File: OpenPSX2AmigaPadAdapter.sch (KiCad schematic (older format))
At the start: 42 parts, among them J1 TO_PSX_PAD, J2 DB9_F, J3 CONN_FTDI, J4 CONN_ICSP, J99 OSHW_LOGO, Q1 BSS138, Q2 BSS138, Q3 BSS138, Q4 BSS138, SW1 RESET, U1 ATmega328P-AU, U2 LM1117-3.3, Y1 16M, Y2 16M

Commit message: Final PCB fixes for V2
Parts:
- renumbered C2 to C1, C8 to C10, C1 to C2, C6 to C3, C7 to C4, C4 to C6, C3 to C7, C9 to C8, C10 to C9, LD2 to LD1, LD1 to LD2, R15 to R11, R14 to R12, R12 to R14, R11 to R15
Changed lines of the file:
@@
 	3545 2685 3465 2685
 $Comp
-L Device:C C8
+L Device:C C10
 U 1 1 5D1C8DC2
 P 3330 2905
-F 0 "C8" V 3280 3005 50  0000 C CNN
+F 0 "C10" V 3280 3030 50  0000 C CNN
 F 1 "100n" V 3385 3055 50  0000 C CNN
 F 2 "Capacitor_SMD:C_0805_2012Metric_Pad1.15x1.40mm_HandSolder" H 3368 2755 50  0001 C CNN
@@
 NoConn ~ 2390 2505
 $Comp
-L Device:LED LD1
+L Device:LED LD2
 U 1 1 5D311FEE
 P 4775 5375
-F 0 "LD1" H 4768 5211 50  0000 C CNN
+F 0 "LD2" H 4768 5211 50  0000 C CNN
 F 1 "LED" H 4768 5211 50  0001 C CNN
 F 2 "LED_SMD:LED_0805_2012Metric_Pad1.15x1.40mm_HandSolder" H 4775 5375 50  0001 C CNN
@@
 	2390 2305 2720 2305
 Text Label 2460 2305 0    50   ~ 0
+led2
+Text Label 2460 2405 0    50   ~ 0
 led1
-Text Label 2460 2405 0    50   ~ 0
-led2
 $Comp
 L power:GND #PWR027
@@
 $EndComp
 $Comp
-L Device:LED LD2
+L Device:LED LD1
 U 1 1 5D332AA0
 P 4775 5575
-F 0 "LD2" H 4768 5699 50  0000 C CNN
+F 0 "LD1" H 4768 5699 50  0000 C CNN
 F 1 "LED" H 4768 5789 50  0001 C CNN
 F 2 "LED_SMD:LED_0805_2012Metric_Pad1.15x1.40mm_HandSolder" H 4775 5575 50  0001 C CNN
@@
 	5075 5575 5075 5670
 $Comp
-L Device:R R11
+L Device:R R15
 U 1 1 5D343268
 P 4340 5375
-F 0 "R11" V 4133 5375 50  0000 C CNN
+F 0 "R15" V 4133 5375 50  0000 C CNN
 F 1 "220" V 4224 5375 50  0000 C CNN
 F 2 "Resistor_SMD:R_0805_2012Metric_Pad1.15x1.40mm_HandSolder" V 4270 5375 50  0001 C CNN
@@
 $EndComp
 $Comp
-L Device:R R12
+L Device:R R14
 U 1 1 5D343E5C
 P 4340 5575
-F 0 "R12" V 4455 5575 50  0000 C CNN
+F 0 "R14" V 4455 5575 50  0000 C CNN
 F 1 "220" V 4546 5575 50  0000 C CNN
 F 2 "Resistor_SMD:R_0805_2012Metric_Pad1.15x1.40mm_HandSolder" V 4270 5575 50  0001 C CNN
@@
 Wire Wire Line
 	4190 5575 3920 5575
-Text Label 3920 5375 0    50   ~ 0
-led1
-Text Label 3920 5575 0    50   ~ 0
-led2
 Wire Wire Line
 	1310 5905 1660 5905
@@
 $EndComp
 $Comp
-L Device:C C4
+L Device:C C6
 U 1 1 5D3D42CF
 P 1310 6205
-F 0 "C4" H 1275 6120 50  0000 R CNN
+F 0 "C6" H 1275 6120 50  0000 R CNN
 F 1 "100n" H 1280 6315 50  0000 R CNN
 F 2 "Capacitor_SMD:C_0805_2012Metric_Pad1.15x1.40mm_HandSolder" H 1348 6055 50  0001 C CNN
@@
 $EndComp
 $Comp
-L Device:C C3
+L Device:C C7
 U 1 1 5D3D4648
 P 1660 6205
-F 0 "C3" H 1620 6120 50  0000 R CNN
+F 0 "C7" H 1620 6120 50  0000 R CNN
 F 1 "100n" H 1625 6315 50  0000 R CNN
 F 2 "Capacitor_SMD:C_0805_2012Metric_Pad1.15x1.40mm_HandSolder" H 1698 6055 50  0001 C CNN
@@
 $EndComp
 $Comp
-L Device:C C1
+L Device:C C2
 U 1 1 5D3DD729
 P 2010 6205
-F 0 "C1" H 1975 6115 50  0000 R CNN
+F 0 "C2" H 1975 6115 50  0000 R CNN
 F 1 "10u" H 1985 6315 50  0000 R CNN
 F 2 "Capacitor_SMD:C_1206_3216Metric_Pad1.42x1.75mm_HandSolder" H 2048 6055 50  0001 C CNN
@@
 $EndComp
 $Comp
-L Device:C C2
+L Device:C C1
 U 1 1 5D3DDD18
 P 3210 6205
-F 0 "C2" H 3175 6115 50  0000 R CNN
+F 0 "C1" H 3175 6115 50  0000 R CNN
 F 1 "10u" H 3175 6320 50  0000 R CNN
 F 2 "Capacitor_SMD:C_1206_3216Metric_Pad1.42x1.75mm_HandSolder" H 3248 6055 50  0001 C CNN
@@
 FOR ICSP
 $Comp
-L Device:C C6
+L Device:C C3
 U 1 1 5D19A701
 P 4205 2005
-F 0 "C6" V 3953 2005 50  0000 C CNN
+F 0 "C3" V 3953 2005 50  0000 C CNN
 F 1 "22p" V 4044 2005 50  0000 C CNN
 F 2 "Capacitor_SMD:C_0805_2012Metric_Pad1.15x1.40mm_HandSolder" H 4243 1855 50  0001 C CNN
@@
 	4510 2305 4510 2505
 $Comp
-L Device:C C7
+L Device:C C4
 U 1 1 5D1A882F
 P 4205 2305
-F 0 "C7" V 4365 2305 50  0000 C CNN
+F 0 "C4" V 4365 2305 50  0000 C CNN
 F 1 "22p" V 4456 2305 50  0000 C CNN
 F 2 "Capacitor_SMD:C_0805_2012Metric_Pad1.15x1.40mm_HandSolder" H 4243 2155 50  0001 C CNN
@@
 	8710 4880 9895 4880
 $Comp
-L Device:R R15
+L Device:R R11
 U 1 1 5DAF3262
 P 9655 1920
-F 0 "R15" H 9820 1770 50  0000 R CNN
+F 0 "R11" H 9820 1770 50  0000 R CNN
 F 1 "10k" V 9655 1990 50  0000 R CNN
 F 2 "Resistor_SMD:R_0805_2012Metric_Pad1.15x1.40mm_HandSolder" V 9585 1920 50  0001 C CNN
@@
 $EndComp
 $Comp
-L Device:R R14
+L Device:R R12
 U 1 1 5DAFD7E8
 P 9395 1930
-F 0 "R14" H 9555 1780 50  0000 R CNN
+F 0 "R12" H 9555 1780 50  0000 R CNN
 F 1 "10k" V 9395 2005 50  0000 R CNN
 F 2 "Resistor_SMD:R_0805_2012Metric_Pad1.15x1.40mm_HandSolder" V 9325 1930 50  0001 C CNN
@@
 	9395 2900 8745 2900
 $Comp
-L Device:C C10
+L Device:C C9
 U 1 1 5DB50106
 P 9655 3235
-F 0 "C10" H 9770 3281 50  0000 L CNN
-F 1 "220p" H 9770 3190 50  0000 L CNN
+F 0 "C9" H 9660 3320 50  0000 L CNN
+F 1 "220p" H 9665 3150 50  0000 L CNN
 F 2 "Capacitor_SMD:C_0805_2012Metric_Pad1.15x1.40mm_HandSolder" H 9693 3085 50  0001 C CNN
 F 3 "~" H 9655 3235 50  0001 C CNN
@@
 $EndComp
 $Comp
-L Device:C C9
+L Device:C C8
 U 1 1 5DB5B8E8
 P 9395 3235
-F 0 "C9" H 9280 3281 50  0000 R CNN
-F 1 "820p" H 9280 3190 50  0000 R CNN
+F 0 "C8" H 9505 3320 50  0000 R CNN
+F 1 "820p" H 9590 3145 50  0000 R CNN
 F 2 "Capacitor_SMD:C_0805_2012Metric_Pad1.15x1.40mm_HandSolder" H 9433 3085 50  0001 C CNN
 F 3 "~" H 9395 3235 50  0001 C CNN
@@
 	9395 3575 9655 3575
 Connection ~ 9655 3575
+Text Label 3920 5575 0    50   ~ 0
+led1
+Text Label 3920 5375 0    50   ~ 0
+led2
 $EndSCHEMATC

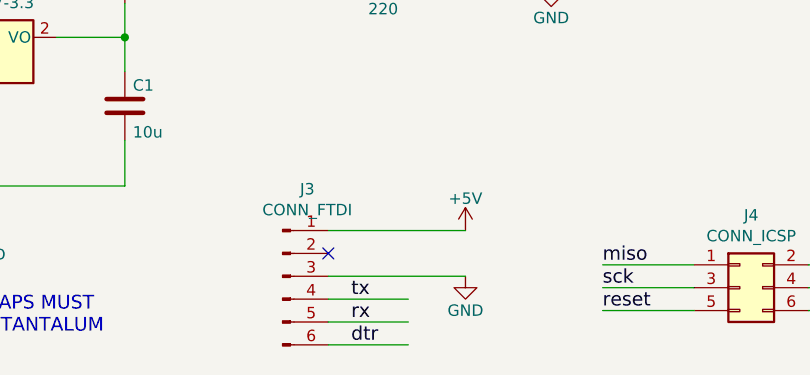
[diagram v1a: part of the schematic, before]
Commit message: Use handsoldering footprints and fix FTDI connector
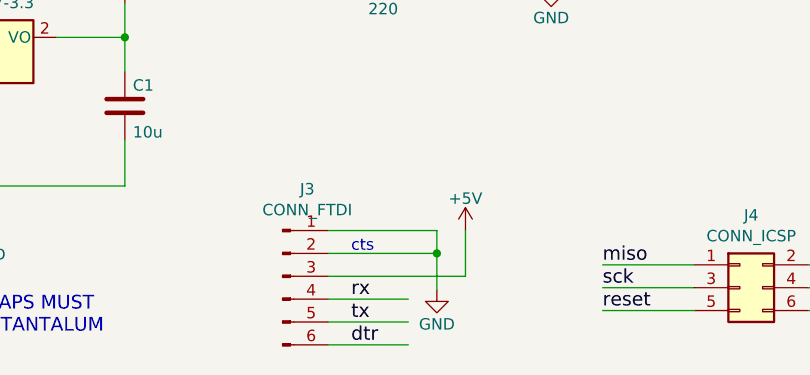
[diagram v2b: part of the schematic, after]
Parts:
- Q1, Q2, Q3, Q4: footprint Package_TO_SOT_SMD:SOT-23 -> Package_TO_SOT_SMD:SOT-23_Handsoldering
- SW1: footprint Button_Switch_SMD:SW_SPST_EVPBF -> Button_Switch_SMD:SW_SPST_EVQQ2
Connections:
- wire segments 189 -> 193
- no-connect marks 11 -> 10
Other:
- note added: "cts"
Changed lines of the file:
@@
 EESchema Schematic File Version 4
-LIBS:OpenPSX2AmigaPadAdapter-cache
-EELAYER 29 0
+EELAYER 30 0
 EELAYER END
 $Descr A4 11693 8268
@@
 Sheet 1 1
 Title "OpenPSX2AmigaPadAdapter"
-Date "2019-10-29"
-Rev "2"
+Date "2019-12-10"
+Rev "3"
 Comp "SukkoPera"
 Comment1 "Licensed under CERN OHL v.1.2"
@@
 $EndComp
 Wire Wire Line
-	4100 6750 4700 6750
-Wire Wire Line
-	4100 6950 4700 6950
+	4100 6750 4575 6750
 Wire Wire Line
 	4100 7050 4450 7050
@@
 Wire Wire Line
 	4100 7250 4450 7250
-NoConn ~ 4100 6850
 $Comp
 L power:+5V #PWR023
@@
 L power:GND #PWR024
 U 1 1 5D19A809
-P 4700 6950
-F 0 "#PWR024" H 4700 6700 50  0001 C CNN
-F 1 "GND" H 4700 6800 50  0000 C CNN
-F 2 "" H 4700 6950 50  0000 C CNN
-F 3 "" H 4700 6950 50  0000 C CNN
-	1    4700 6950
-	1    0    0    -1
-$EndComp
-Text Label 4200 7050 0    60   ~ 0
+P 4575 7010
+F 0 "#PWR024" H 4575 6760 50  0001 C CNN
+F 1 "GND" H 4575 6860 50  0000 C CNN
+F 2 "" H 4575 7010 50  0000 C CNN
+F 3 "" H 4575 7010 50  0000 C CNN
+	1    4575 7010
+	1    0    0    -1
+$EndComp
+Text Label 4200 7150 0    60   ~ 0
 tx
-Text Label 4200 7150 0    60   ~ 0
-rx
 Text Label 4200 7250 0    60   ~ 0
 dtr
@@
 F 0 "Q1" V 7001 1850 50  0000 C CNN
 F 1 "BSS138" V 7092 1850 50  0000 C CNN
-F 2 "Package_TO_SOT_SMD:SOT-23" H 6950 1775 50  0001 L CIN
+F 2 "Package_TO_SOT_SMD:SOT-23_Handsoldering" H 6950 1775 50  0001 L CIN
 F 3 "https://www.fairchildsemi.com/datasheets/BS/BSS138.pdf" H 6750 1850 50  0001 L CNN
 	1    6750 1850
@@
 F 0 "Q2" V 7001 3100 50  0000 C CNN
 F 1 "BSS138" V 7092 3100 50  0000 C CNN
-F 2 "Package_TO_SOT_SMD:SOT-23" H 6950 3025 50  0001 L CIN
+F 2 "Package_TO_SOT_SMD:SOT-23_Handsoldering" H 6950 3025 50  0001 L CIN
 F 3 "https://www.fairchildsemi.com/datasheets/BS/BSS138.pdf" H 6750 3100 50  0001 L CNN
 	1    6750 3100
@@
 F 0 "Q3" V 7001 4300 50  0000 C CNN
 F 1 "BSS138" V 7092 4300 50  0000 C CNN
-F 2 "Package_TO_SOT_SMD:SOT-23" H 6950 4225 50  0001 L CIN
+F 2 "Package_TO_SOT_SMD:SOT-23_Handsoldering" H 6950 4225 50  0001 L CIN
 F 3 "https://www.fairchildsemi.com/datasheets/BS/BSS138.pdf" H 6750 4300 50  0001 L CNN
 	1    6750 4300
@@
 F 0 "Q4" V 7001 5550 50  0000 C CNN
 F 1 "BSS138" V 7092 5550 50  0000 C CNN
-F 2 "Package_TO_SOT_SMD:SOT-23" H 6950 5475 50  0001 L CIN
+F 2 "Package_TO_SOT_SMD:SOT-23_Handsoldering" H 6950 5475 50  0001 L CIN
 F 3 "https://www.fairchildsemi.com/datasheets/BS/BSS138.pdf" H 6750 5550 50  0001 L CNN
 	1    6750 5550
@@
 F 0 "SW1" H 4030 3375 50  0000 C CNN
 F 1 "RESET" H 4030 3284 50  0000 C CNN
-F 2 "Button_Switch_SMD:SW_SPST_EVPBF" H 4030 3290 50  0001 C CNN
+F 2 "Button_Switch_SMD:SW_SPST_EVQQ2" H 4030 3290 50  0001 C CNN
 F 3 "~" H 4030 3290 50  0001 C CNN
 	1    4030 3090
@@
 Text Label 3920 5375 0    50   ~ 0
 led2
+Wire Wire Line
+	4700 6950 4700 6750
+Wire Wire Line
+	4575 6750 4575 6850
+Wire Wire Line
+	4100 6950 4700 6950
+Wire Wire Line
+	4100 6850 4575 6850
+Connection ~ 4575 6850
+Wire Wire Line
+	4575 6850 4575 7010
+Text Notes 4200 6850 0    50   ~ 0
+cts
+Text Label 4200 7050 0    60   ~ 0
+rx
 $EndSCHEMATC

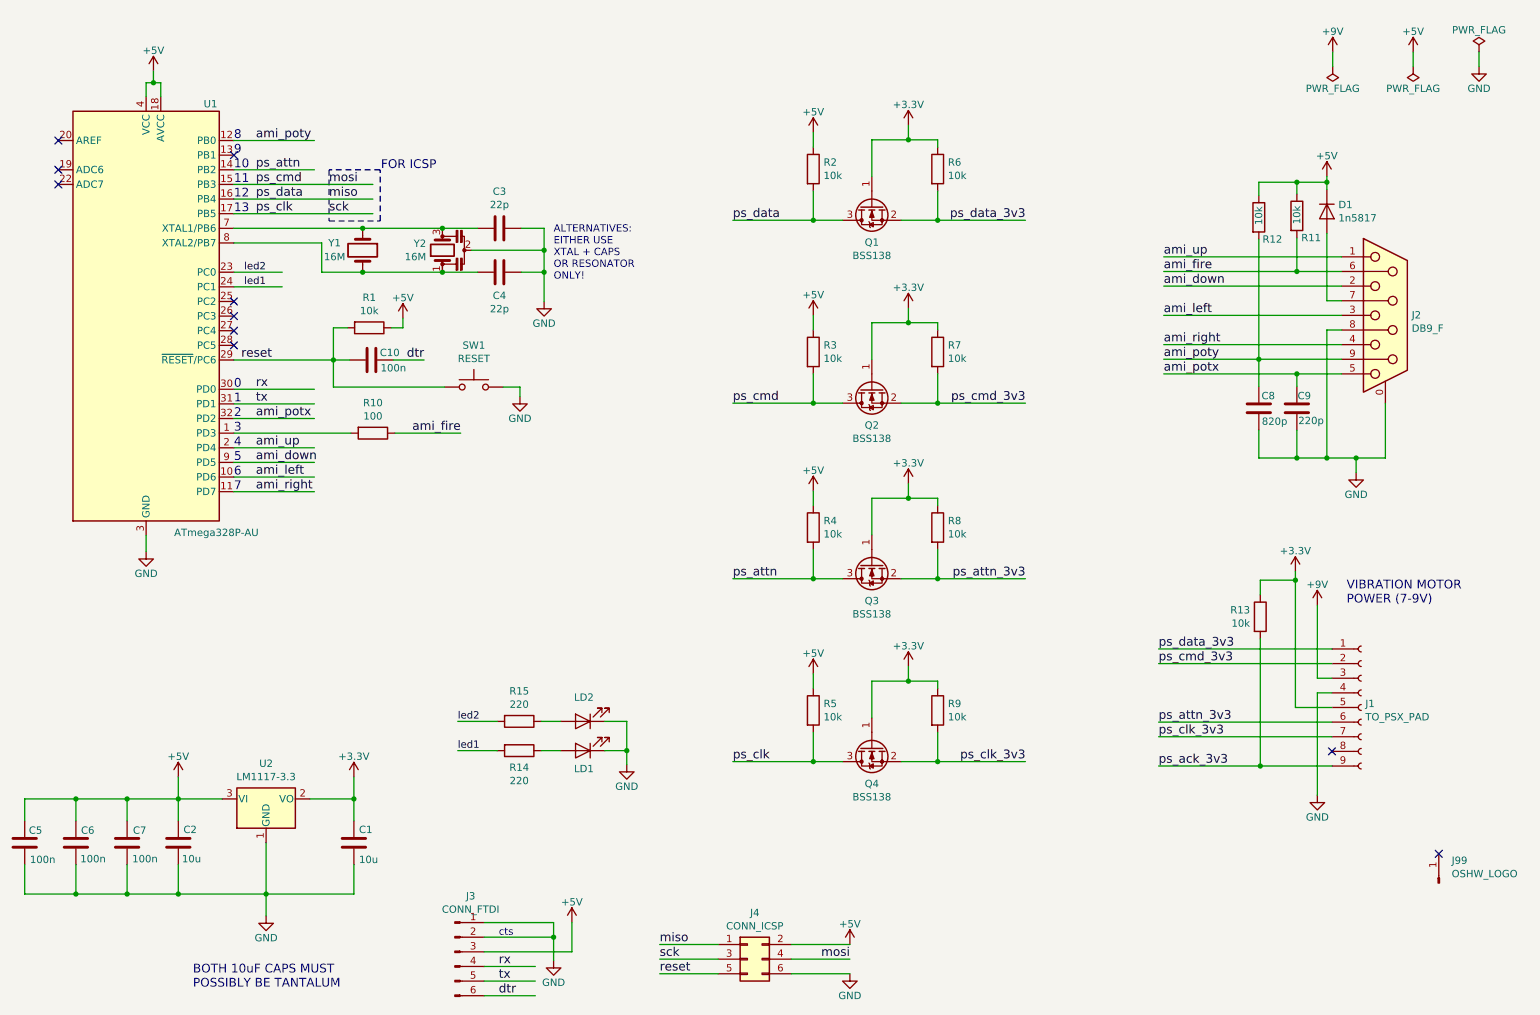
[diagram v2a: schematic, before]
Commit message: Connect ACK signal and remove RESET button
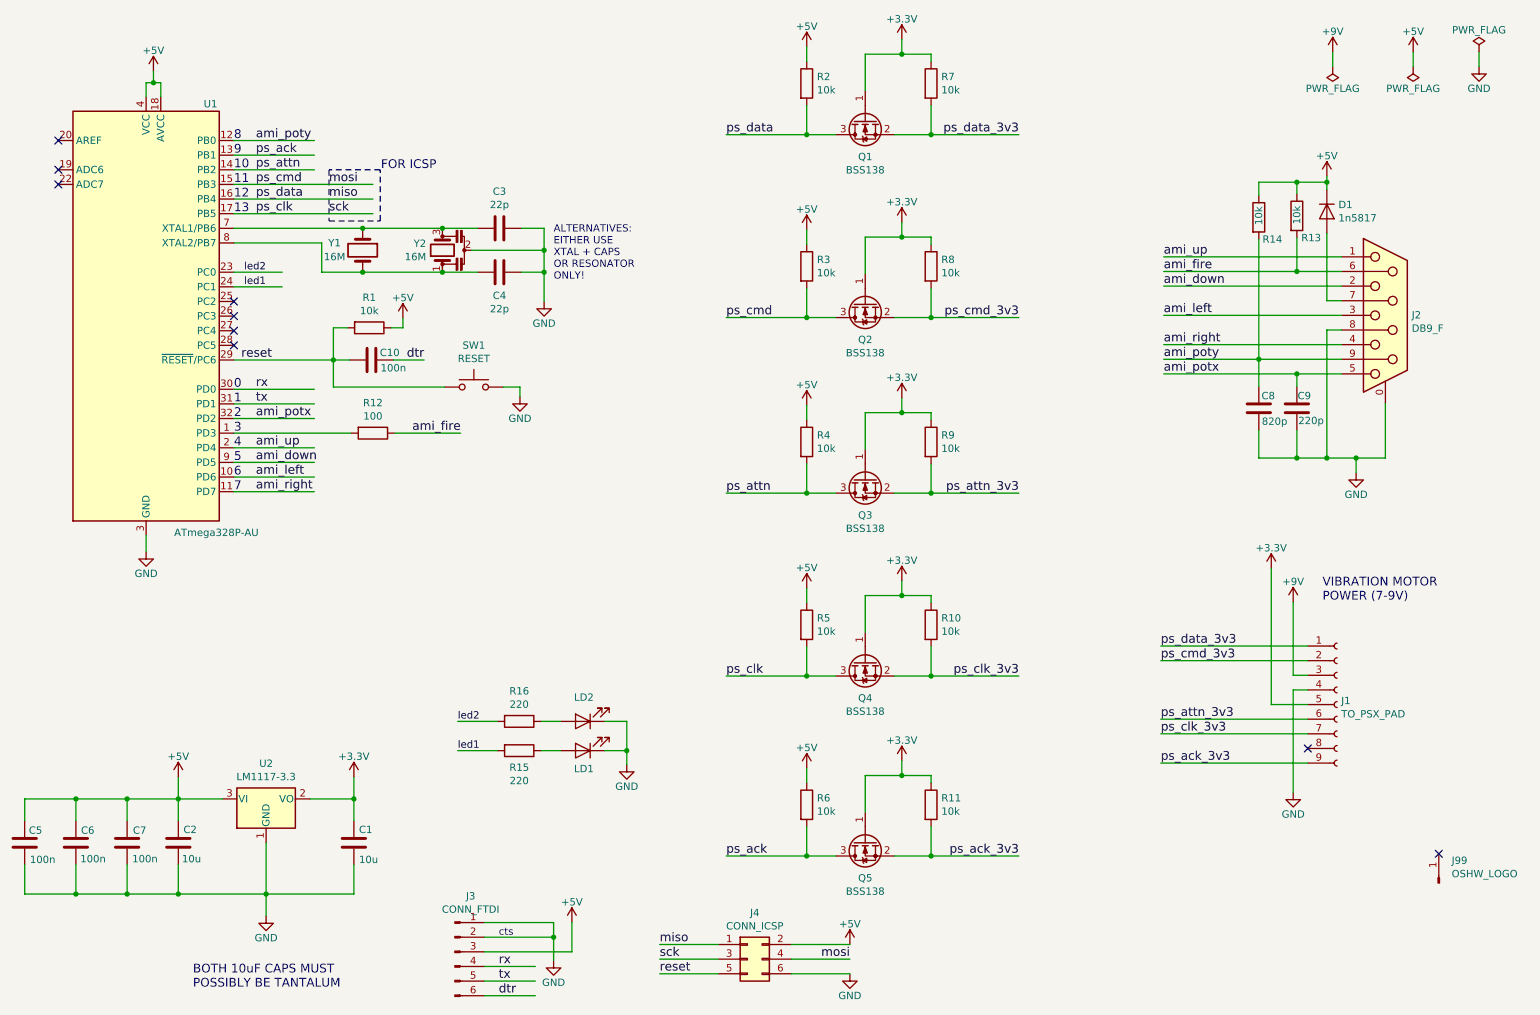
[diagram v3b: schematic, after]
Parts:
- removed R13: 10k, Resistor_SMD:R_0805_2012Metric_Pad1.15x1.40mm_HandSolder, symbol Device:R
- added Q5: BSS138, Package_TO_SOT_SMD:SOT-23_Handsoldering, symbol Transistor_FET:BSS138
- added R11, R6: 10k, Resistor_SMD:R_0805_2012Metric_Pad1.15x1.40mm_HandSolder, symbol Device:R
- SW1: footprint Button_Switch_SMD:SW_SPST_EVQQ2 -> (none)
- Y2: footprint Crystal:Resonator_SMD_muRata_CSTxExxV-3Pin_3.0x1.1mm -> OpenPSX2AmigaPadAdapter:Resonator_SMD_muRata_CSTxExxV
- renumbered R9 to R10, R10 to R12, R11 to R13, R12 to R14, R14 to R15, R15 to R16, R6 to R7, R7 to R8, R8 to R9
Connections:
- net labels added: ps_ack
- wire segments 193 -> 201
- no-connect marks 10 -> 9
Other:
- moved on the sheet: J1, Q1, Q2, Q3, Q4, R10, R2, R3, R4, R5, R7, R8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
